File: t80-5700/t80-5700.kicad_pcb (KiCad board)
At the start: 2 copper layers, 81 x 130.6 mm, 94 parts, among them J1 USB_C_Receptacle_USB2.0, J2 Conn_01x05, U1 RP2040, U2 W25Q128JVS, U3 XC6206PxxxMR, U4 SRV05-4, Y1 Crystal_GND24

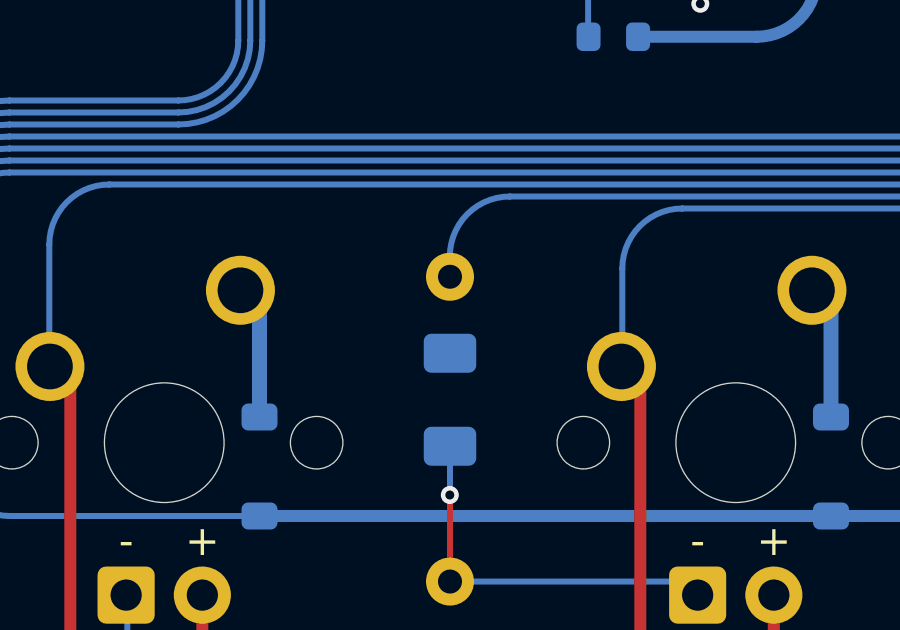
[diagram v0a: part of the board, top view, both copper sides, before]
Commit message: fix noncritical missing trace on 5700
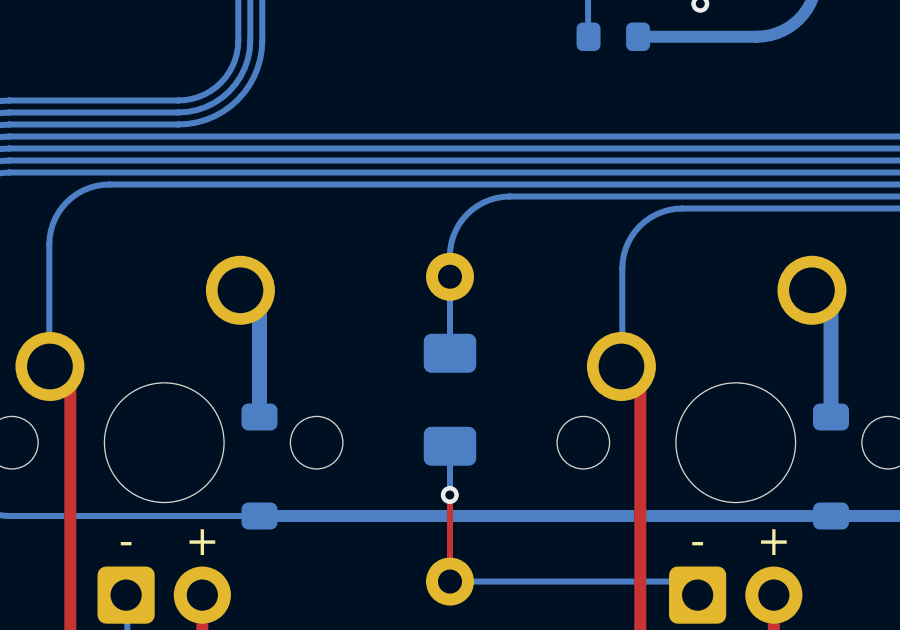
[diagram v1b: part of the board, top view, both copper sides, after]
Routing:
- net LED_DIV: track 43.5 -> 46.0 mm
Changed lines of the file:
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@@
 		(fp_arc
 			(start 14.78125 -8.000001)
-			(mid 15.134771 -7.853537)
+			(mid 15.134807 -7.853543)
 			(end 15.28125 -7.500001)
 			(stroke
@@
 		(fp_arc
 			(start 9.03125 5.999999)
-			(mid 8.677729 5.853535)
+			(mid 8.677694 5.853541)
 			(end 8.53125 5.499999)
 			(stroke
@@
 		(fp_arc
 			(start 14.78125 -8.000001)
-			(mid 15.134771 -7.853537)
+			(mid 15.134807 -7.853543)
 			(end 15.28125 -7.500001)
 			(stroke
@@
 		(fp_arc
 			(start 9.03125 5.999999)
-			(mid 8.677729 5.853535)
+			(mid 8.677694 5.853541)
 			(end 8.53125 5.499999)
 			(stroke
@@
 		(fp_arc
 			(start 14.78125 -8.000001)
-			(mid 15.134771 -7.853537)
+			(mid 15.134807 -7.853543)
 			(end 15.28125 -7.500001)
 			(stroke
@@
 		(fp_arc
 			(start 9.03125 5.999999)
-			(mid 8.677729 5.853535)
+			(mid 8.677694 5.853541)
 			(end 8.53125 5.499999)
 			(stroke
@@
 		(fp_arc
 			(start 14.78125 -8.000001)
-			(mid 15.134771 -7.853537)
+			(mid 15.134807 -7.853543)
 			(end 15.28125 -7.500001)
 			(stroke
@@
 		(fp_arc
 			(start 9.03125 5.999999)
-			(mid 8.677729 5.853535)
+			(mid 8.677694 5.853541)
 			(end 8.53125 5.499999)
 			(stroke
@@
 		(width 0.2)
 		(layer "B.Cu")
+		(net 43)
+	)
+	(segment
+		(start 69.05625 56.55)
+		(end 69.05625 54)
+		(width 0.2)
+		(layer "B.Cu")
